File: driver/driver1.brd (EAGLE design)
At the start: 86 x 68.6 mm, 86 parts, among them IC3 74HC14N, IC4 74HC08N, IC5 74HC74N

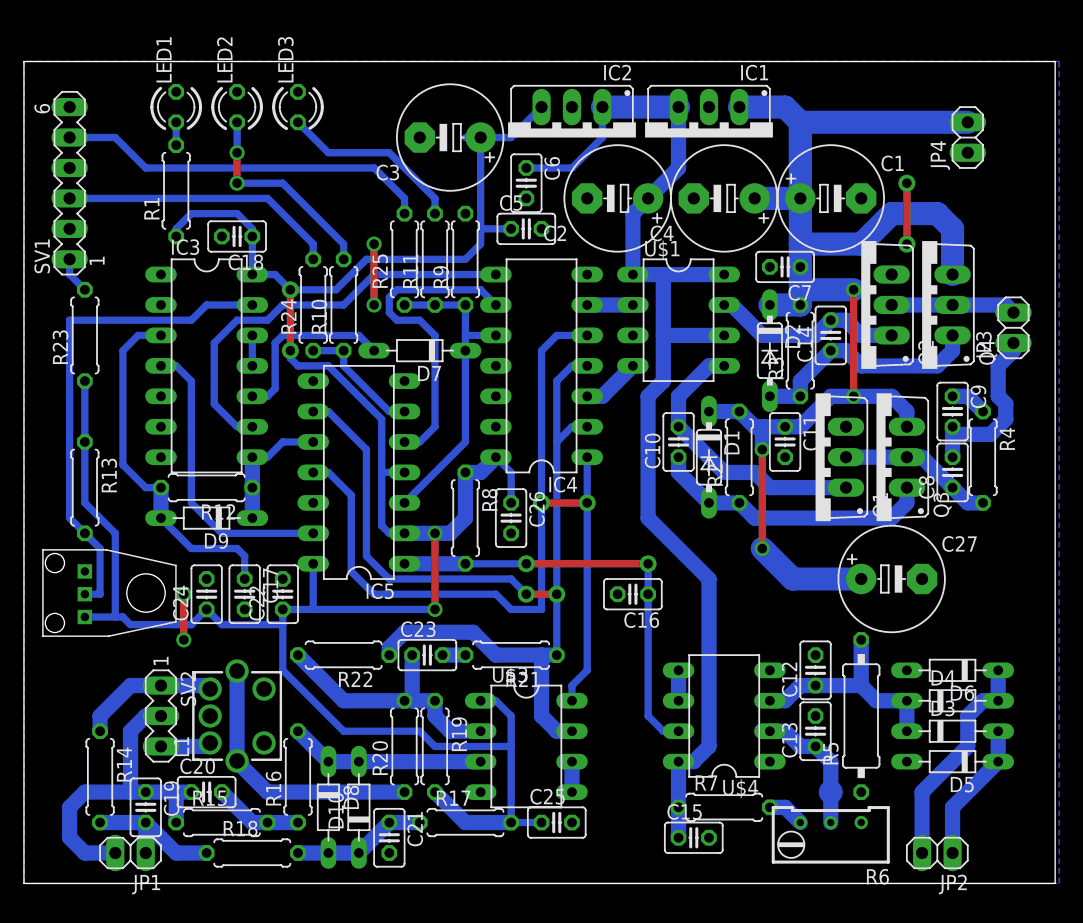
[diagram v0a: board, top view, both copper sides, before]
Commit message: improved board layout for use with recom switching 78xx regulators
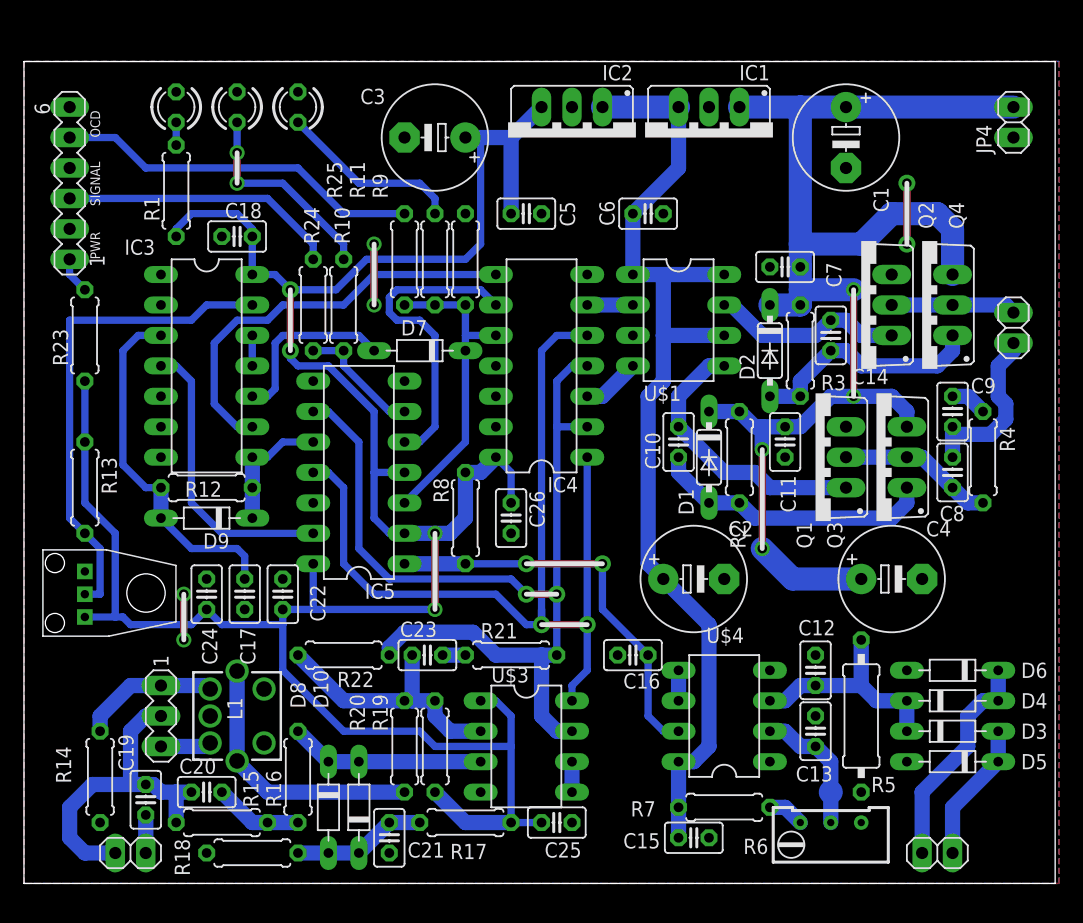
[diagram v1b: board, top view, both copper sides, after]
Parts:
- removed C27: 470u, rcl:E5-8,5
- moved C4 34.7 mm to (72.4, 25.4), turned to 0 degrees
- moved C2 32.4 mm to (55.9, 25.4), turned to 0 degrees
- moved C6 10.5 mm to (52.1, 55.9), turned to 0 degrees
- moved C1 5.24 mm to (68.6, 62.2), turned to 270 degrees
- moved C16 5.08 mm to (50.8, 19.1)
- moved JP4 4.02 mm to (82.5, 63.5)
- moved C3 1.27 mm to (34.3, 62.2)
- moved C5 1.27 mm to (41.9, 55.9)
- moved C19 0.64 mm to (10.2, 6.99)
- renumbered SV1 to LED
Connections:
- net +24V: no longer C27.+
- net GND: no longer C27.-
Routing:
- net +9V: track 96.0 -> 86.0 mm
- net GND: track 51.6 -> 42.3 mm
- net +5V: track 207.1 -> 211.6 mm
- net N$34: track 78.1 -> 81.2 mm
- net N$13: track 36.1 -> 33.9 mm
- net +24V: track 111.9 -> 112.7 mm
- net N$18: track 31.3 -> 30.6 mm
- net N$7: track 84.9 -> 84.4 mm
- added copper zone on layer 1, net GND
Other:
- board text added: "OCD"
- board text added: "PWR"
- board text added: "SIGNAL"

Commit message: further pcb optimizations
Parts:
- moved LED3 20.1 mm to (3.81, 58.4)
- moved LED 17.0 mm to (19.1, 66.0), turned to 0 degrees
- moved R23 15.4 mm to (12.7, 59.1)
- moved LED1 14.5 mm to (3.81, 53.3)
- moved R1 14.3 mm to (5.08, 45.7)
- moved LED2 14.0 mm to (3.81, 63.5)
- moved C16 7.73 mm to (49.5, 11.4), turned to 270 degrees
- moved R25 5.85 mm to (35.6, 56.5), turned to 180 degrees
- moved C5 3.81 mm to (41.9, 59.7)
- moved R10 2.84 mm to (24.1, 49.5)
- moved R24 2.84 mm to (26.7, 49.5)
- moved C8 2.54 mm to (77.5, 36.8)
- moved R11 2.29 mm to (33.0, 50.2)
- moved R9 2.29 mm to (35.6, 50.2)
- moved C9 1.80 mm to (78.7, 40.6), turned to 180 degrees
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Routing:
- net GND: track 42.3 -> 22.9 mm
- net N$30: track 15.3 -> 33.7 mm
- net N$18: track 30.6 -> 13.2 mm
- net N$25: track 26.2 -> 36.3 mm
- net N$29: track 17.3 -> 24.7 mm, vias 2 -> 0
- net N$35: track 28.1 -> 21.1 mm
- net N$16: track 23.2 -> 16.4 mm
- net +5V: track 211.6 -> 205.3 mm
- net N$9: track 14.7 -> 8.56 mm
- net N$31: track 26.2 -> 21.2 mm
- net +24V: track 112.7 -> 109.8 mm
- net N$27: track 15.0 -> 17.3 mm
- net N$26: track 40.9 -> 38.7 mm
- net N$4: track 13.0 -> 15.0 mm
- net N$12: track 10.4 -> 9.15 mm
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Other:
- board size 86 x 68.6 mm -> 83.5 x 68.6 mm

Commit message: guess what.. pcb improvements
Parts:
- R14: device rcl:0207/7 -> rcl:0309/12
- moved C24 12.8 mm to (3.81, 18.4), turned to 180 degrees
- moved R13 12.8 mm to (6.35, 45.7)
- moved R1 10.9 mm to (11.4, 54.6), turned to 180 degrees
- moved R20 5.39 mm to (27.9, 15.2), turned to 0 degrees
- moved C21 4.02 mm to (34.3, 2.54), turned to 0 degrees
- moved R23 3.59 mm to (10.2, 61.6)
- moved D8 2.54 mm to (27.9, 6.35)
- moved D10 2.54 mm to (30.5, 6.35)
- moved R16 2.54 mm to (25.4, 8.89)
- moved C17 2.29 mm to (16.5, 25.4)
- moved C22 1.80 mm to (20.3, 25.4), turned to 270 degrees
- moved R14 1.27 mm to (3.81, 8.89)
- moved C18 1.27 mm to (19.1, 54.0), turned to 0 degrees
- moved R22 1.27 mm to (27.9, 19.1)
- moved SV2 1.27 mm to (8.89, 14.0)
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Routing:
- net GND: track 22.9 -> 69.8 mm, vias 6 -> 18
- net N$30: track 33.7 -> 38.4 mm
- net +5V: track 205.3 -> 209.3 mm, vias 4 -> 2
- net N$40: track 16.3 -> 13.8 mm
- net N$37: track 8.67 -> 11.2 mm
- net N$26: track 38.7 -> 36.4 mm
- net N$39: track 5.12 -> 7.02 mm
- net N$2: track 3.07 -> 4.86 mm
- net N$7: track 84.4 -> 86.2 mm
- net N$18: track 13.2 -> 14.7 mm
- net N$41: track 11.2 -> 12.7 mm
- net N$47: track 22.4 -> 21.2 mm
- net N$29: track 24.7 -> 25.9 mm
- net N$38: track 11.5 -> 12.4 mm
- net N$35: track 21.1 -> 21.9 mm
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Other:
- board size 83.5 x 68.6 mm -> 83.5 x 69.8 mm
- board text removed: "OCD"
- board text removed: "PWR"
- board text removed: "SIGNAL"

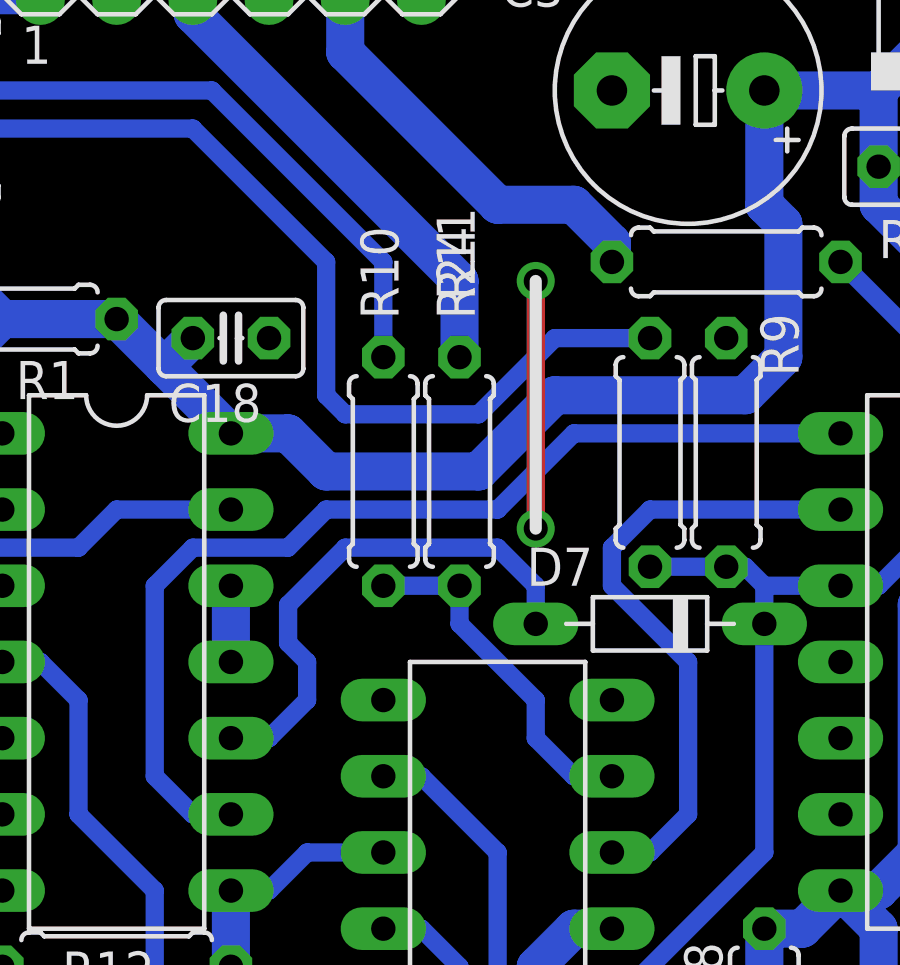
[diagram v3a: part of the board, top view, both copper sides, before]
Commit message: added part values
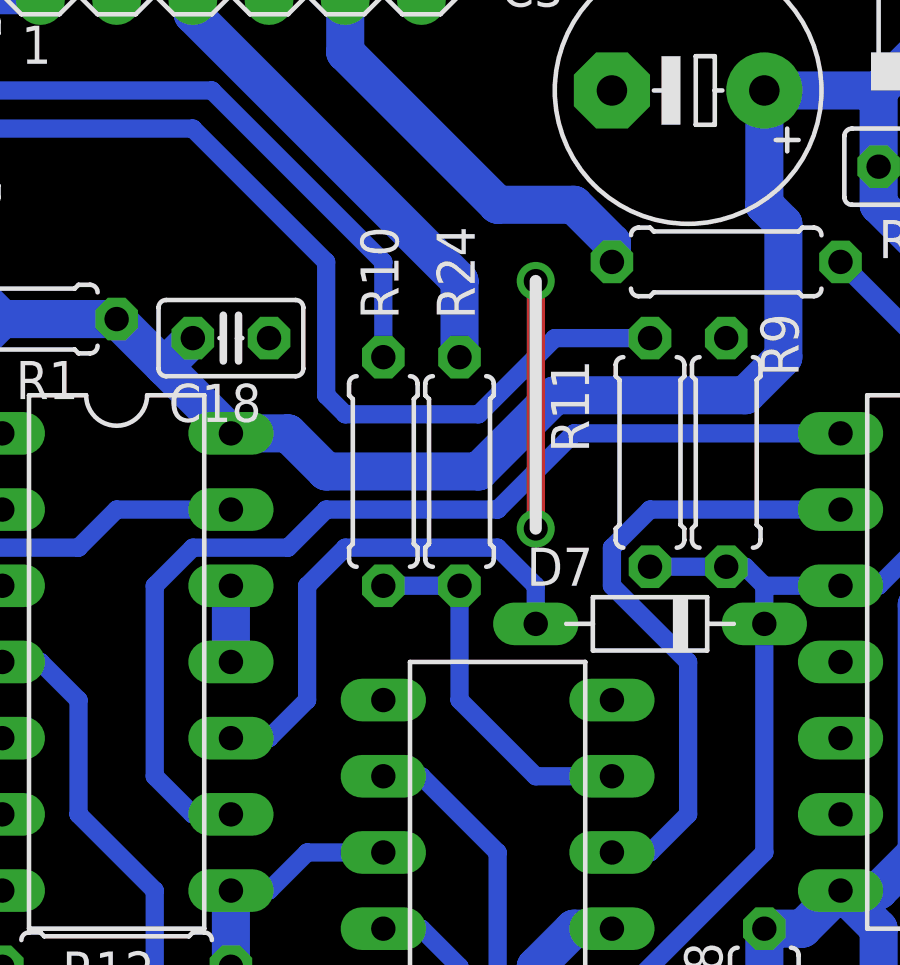
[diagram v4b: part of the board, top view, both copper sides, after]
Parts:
- C11, C7: value 100n -> 4.7u
- C12, C16, C23: value 100n -> 1n
- C13, C22, C9: value 100n -> 1u
- C17: value 100n -> 10n
- C19: value 100n -> 150p
- C8: value 100n -> 2.2u
- R12: value 470R -> 10k
- R13, R16, R17, R19, R2, R3, R8, R9: value 470R -> 1k
- R14: value 470R -> 51
- R15, R22: value 470R -> 100k
- R4: value 470R -> 15
- R5: value 470R -> 5.1
- R6: value (none) -> 10k
- R7: value 470R -> 1.8k
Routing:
- net N$28: track 11.7 -> 12.5 mm
- net N$27: track 17.3 -> 16.8 mm

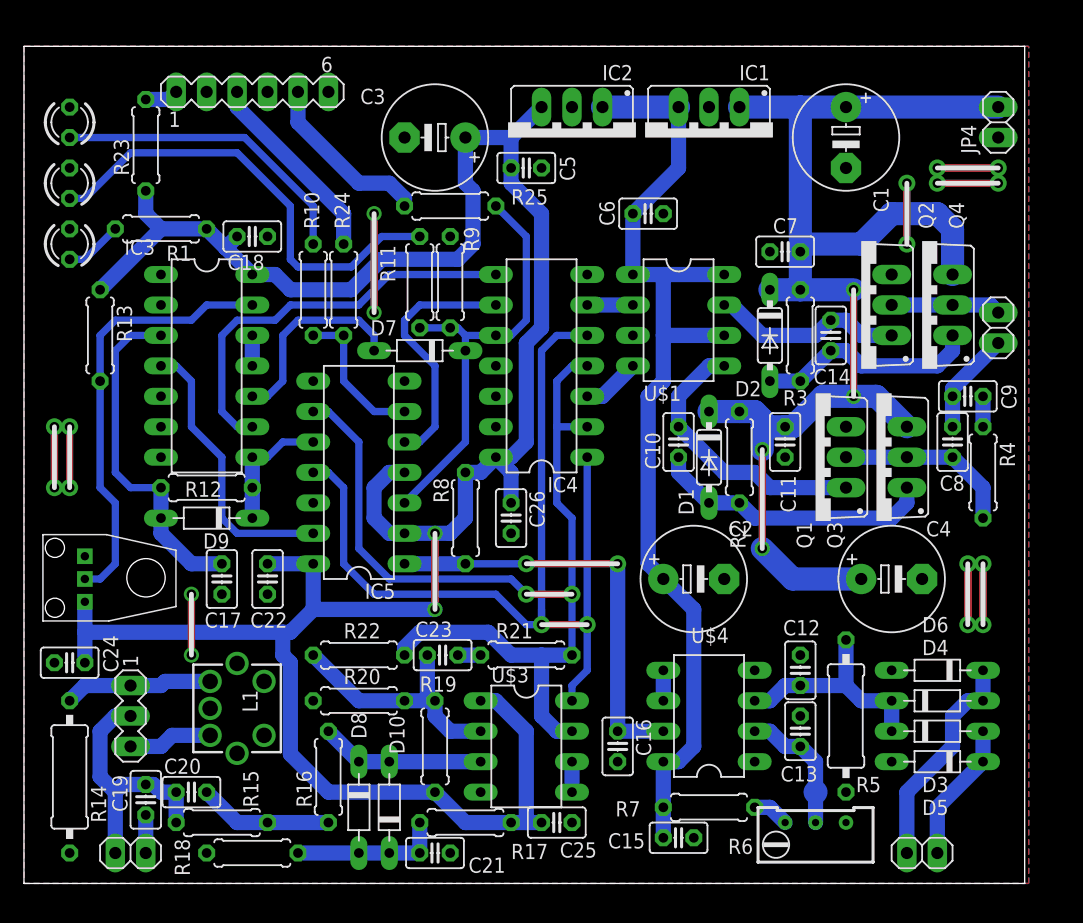
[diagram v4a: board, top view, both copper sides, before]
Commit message: added missing prefix to libraries
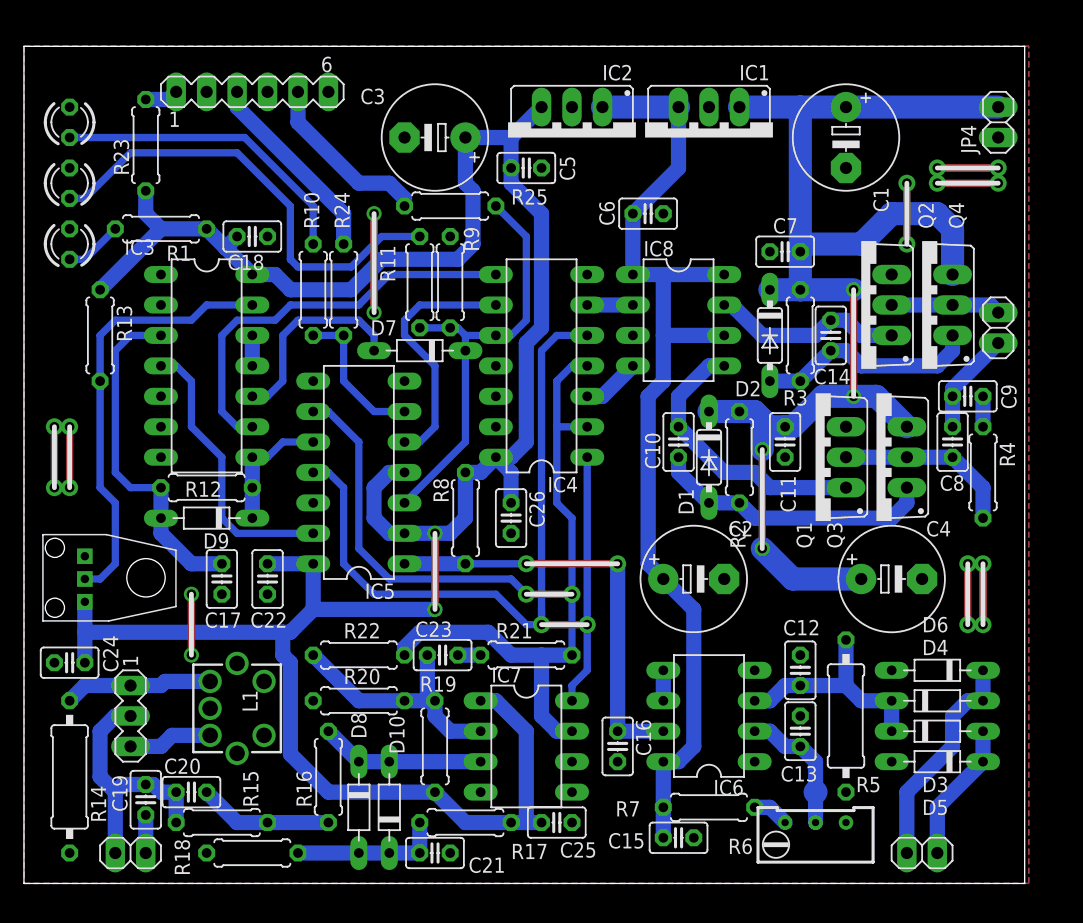
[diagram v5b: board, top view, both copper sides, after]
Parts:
- renumbered U$1 to IC8, U$2 to OP1, U$3 to IC7, U$4 to IC6
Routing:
- net GND: track 69.8 -> 52.1 mm
